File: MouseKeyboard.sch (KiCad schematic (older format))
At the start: 8 parts, among them J1 USB, U1 2AxisPotWSelect

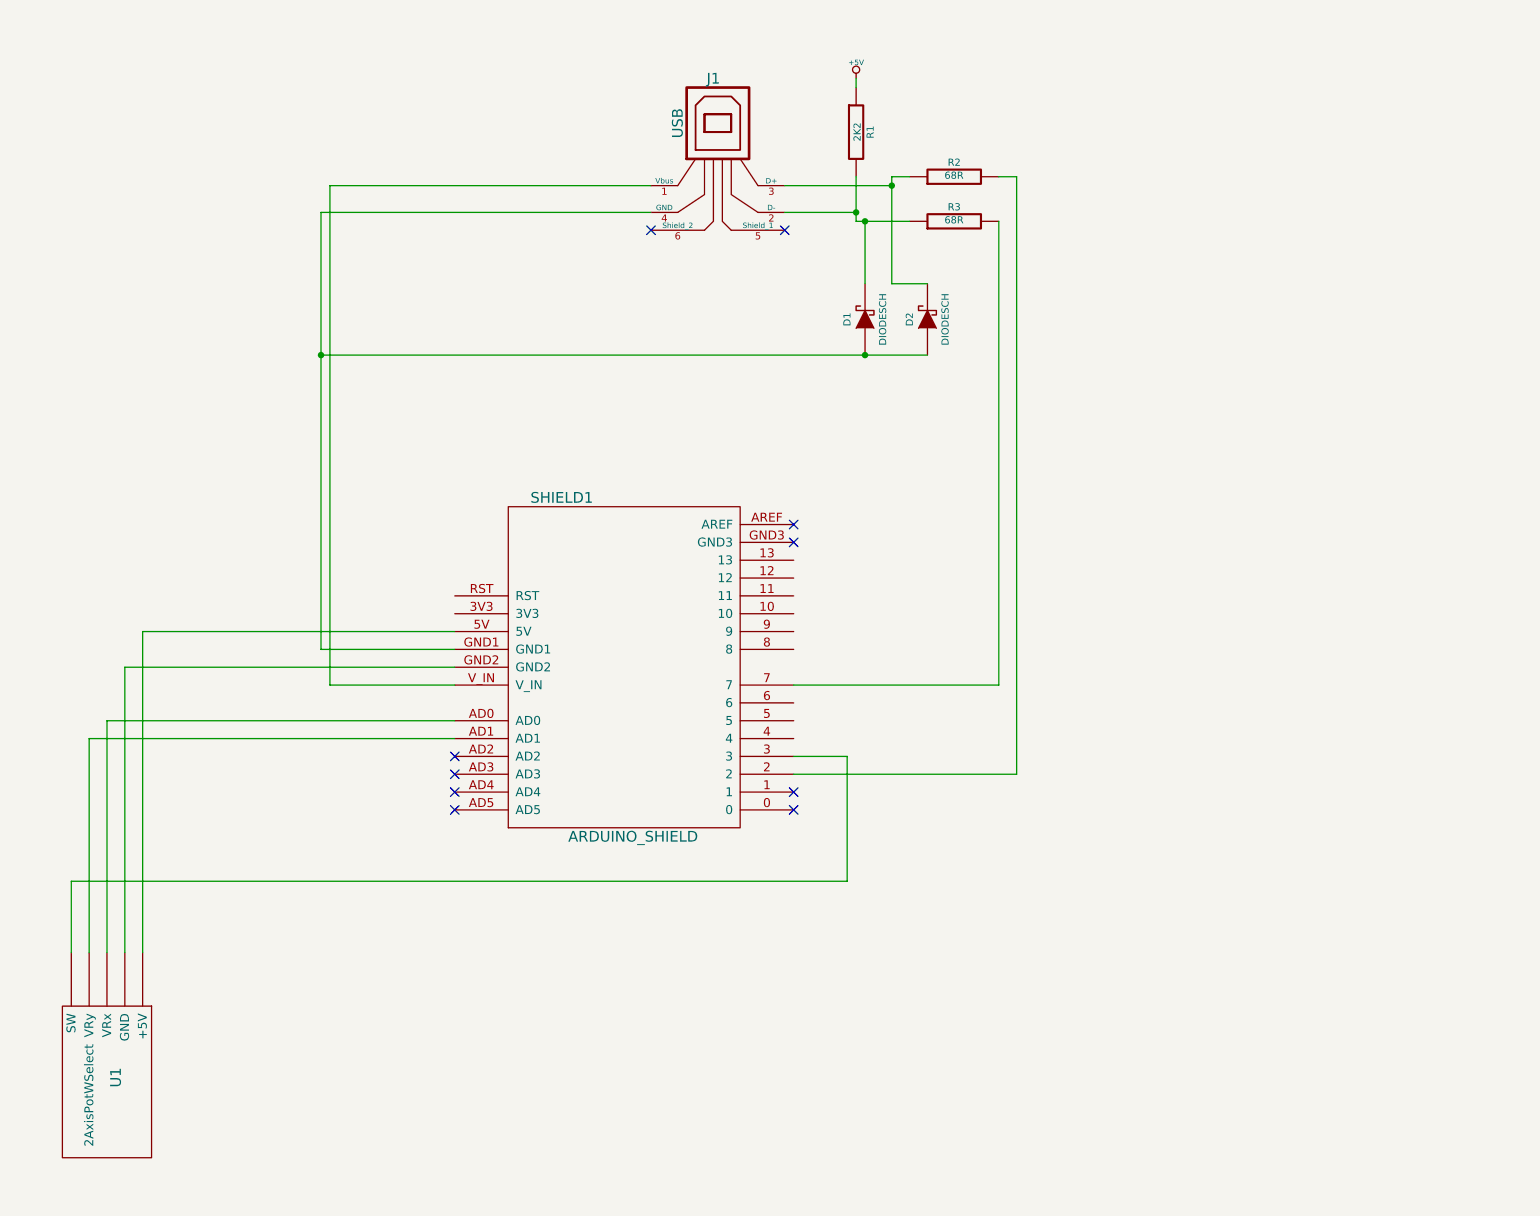
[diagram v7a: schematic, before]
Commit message: Added to the schematic, switches, on/off, etc
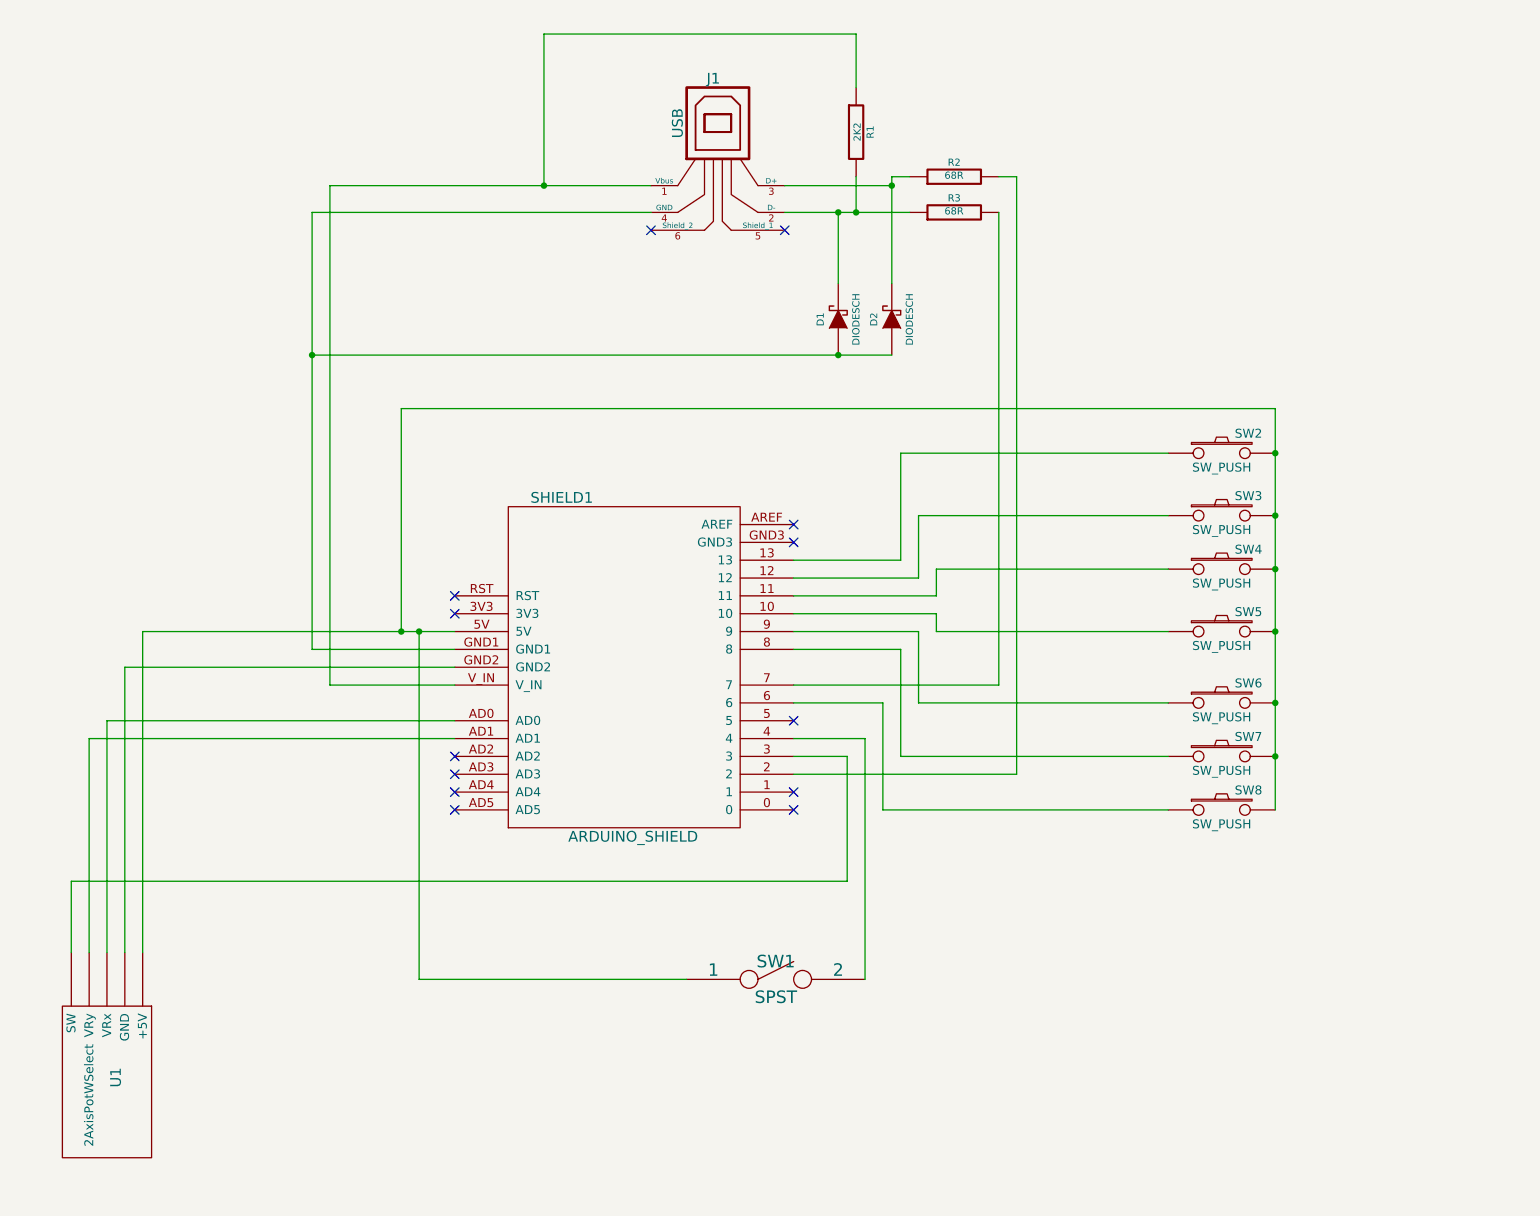
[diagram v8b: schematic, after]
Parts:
- added SW1: SPST, symbol SPST
- added SW2, SW3, SW4, SW5, SW6, SW7, SW8: SW_PUSH, symbol SW_PUSH
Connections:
- net +5V is gone; now on an unnamed net: R1.1
- net at SHIELD1.10: now also SW5.1
- net at SHIELD1.11: now also SW4.1
- net at SHIELD1.12: now also SW3.1
- net at SHIELD1.13: now also SW2.1
- net at SHIELD1.4: now also SW1.2
- net at SHIELD1.5V, U1.~ (VRy): now also SW1.1, SW2.2, SW3.2, SW4.2, SW5.2, SW6.2, SW7.2, SW8.2
- net at SHIELD1.6: now also SW8.1
- net at SHIELD1.8: now also SW7.1
- net at SHIELD1.9: now also SW6.1
- no-connect marks 10 -> 13
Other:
- moved on the sheet: D1, D2, R3
